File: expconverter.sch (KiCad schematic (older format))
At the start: 23 parts, among them IC2 LM324, IC4 LM324, P1 100k, P2 100k, P3 100k log, P7 200, P8 100k

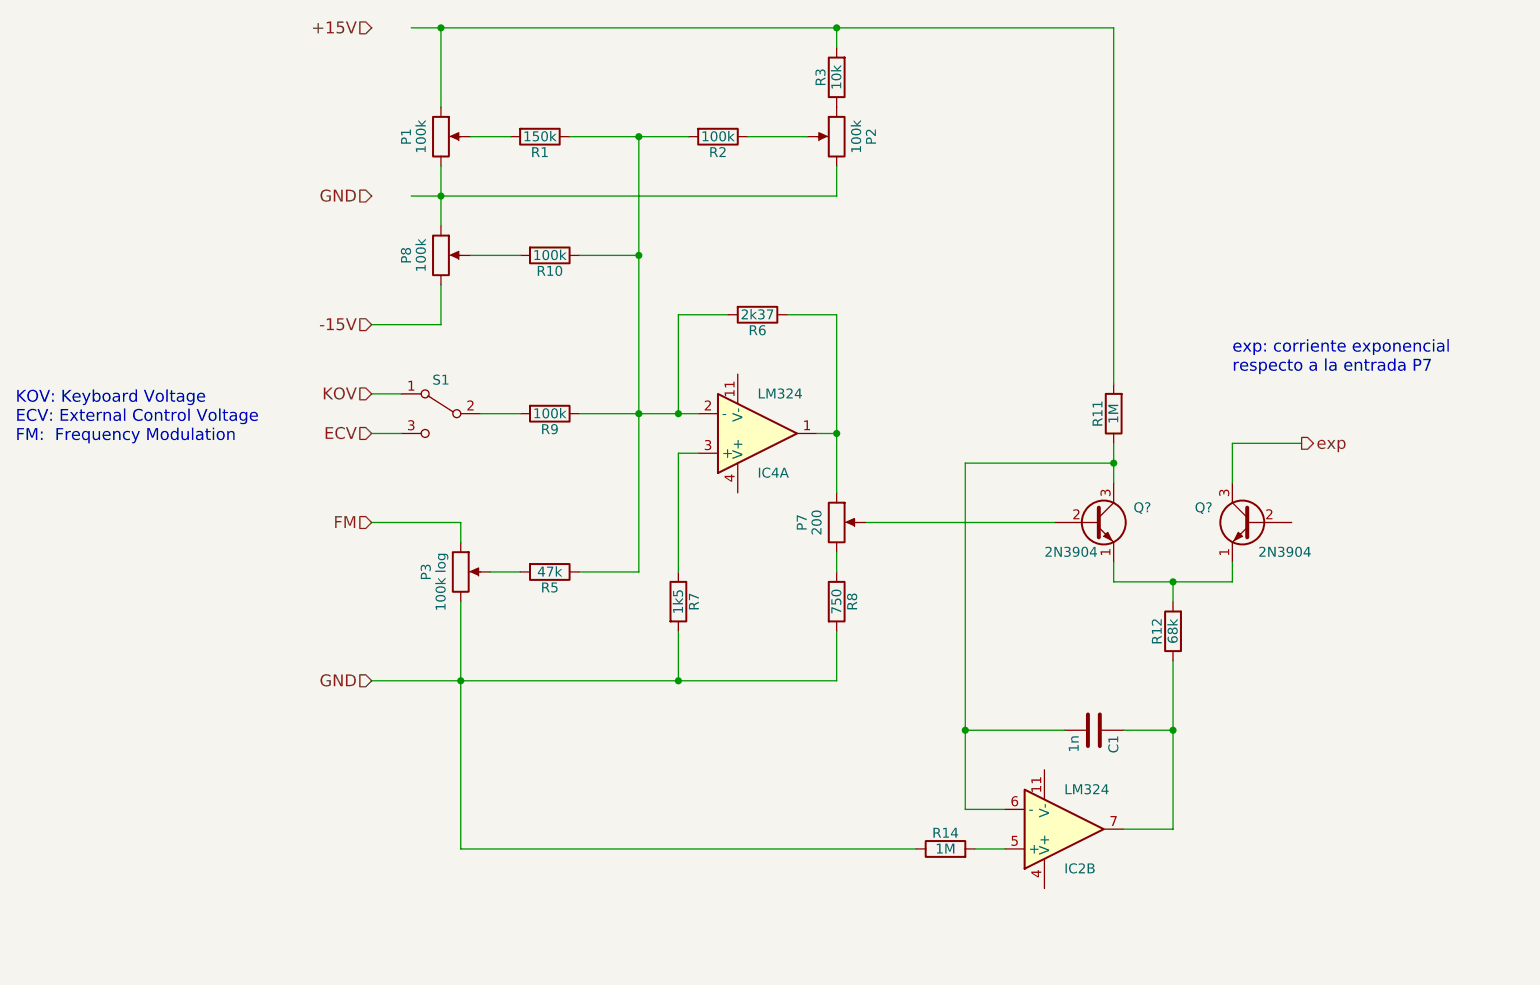
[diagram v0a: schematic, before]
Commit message: sawtooh 2 triangle
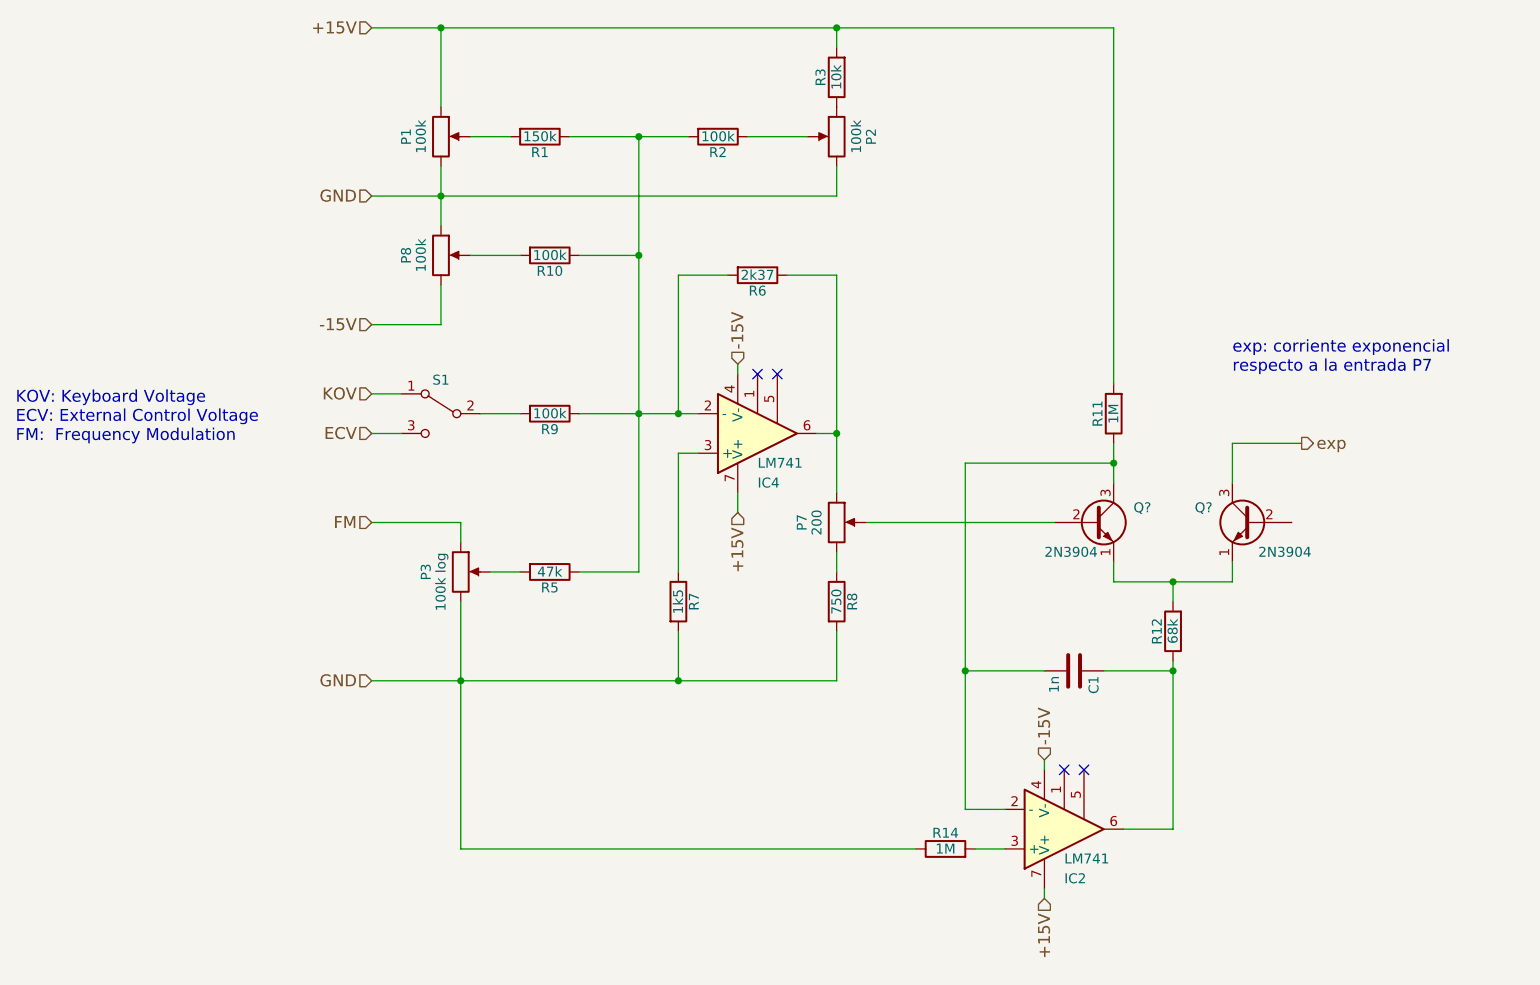
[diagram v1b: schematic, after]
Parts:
- removed IC2, IC4: LM324, symbol LM324
- added IC2, IC4: LM741, symbol LM741
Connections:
- wire segments 53 -> 57
- no-connect marks 0 -> 4
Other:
- moved on the sheet: C1, R6
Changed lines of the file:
@@
 $EndDescr
-$Comp
-L LM324 IC4
-U 1 1 59D555A7
-P 6800 3400
-F 0 "IC4" H 6800 3600 50  0000 L CNN
-F 1 "LM324" H 6800 3200 50  0000 L CNN
-F 2 "" H 6750 3500 50  0001 C CNN
-F 3 "" H 6850 3600 50  0001 C CNN
-	1    6800 3400
-	1    0    0    1
-$EndComp
 $Comp
 L R R6
 U 1 1 59D555CD
-P 6800 2800
-F 0 "R6" V 6880 2800 50  0000 C CNN
-F 1 "2k37" V 6800 2800 50  0000 C CNN
-F 2 "" V 6730 2800 50  0001 C CNN
-F 3 "" H 6800 2800 50  0001 C CNN
-	1    6800 2800
+P 6800 2600
+F 0 "R6" V 6880 2600 50  0000 C CNN
+F 1 "2k37" V 6800 2600 50  0000 C CNN
+F 2 "" V 6730 2600 50  0001 C CNN
+F 3 "" H 6800 2600 50  0001 C CNN
+	1    6800 2600
 	0    1    1    0
 $EndComp
@@
 	4850 3200 5000 3200
 Wire Wire Line
-	6650 2800 6400 2800
-Wire Wire Line
-	6400 2800 6400 3300
+	6650 2600 6400 2600
+Wire Wire Line
+	6400 2600 6400 3300
 Connection ~ 6400 3300
 Wire Wire Line
-	6950 2800 7200 2800
-Wire Wire Line
-	7200 2800 7200 3700
+	6950 2600 7200 2600
+Wire Wire Line
+	7200 2600 7200 3700
 Wire Wire Line
 	7200 3400 7100 3400
@@
 	5200 2050 5200 2350
 Wire Wire Line
-	5050 2200 7200 2200
+	4850 2200 7200 2200
 Connection ~ 5200 2200
 Wire Wire Line
@@
 	5200 1750 5200 1350
 Wire Wire Line
-	5050 1350 8600 1350
+	4850 1350 8600 1350
 Wire Wire Line
 	7200 1350 7200 1450
@@
 $EndComp
 $Comp
-L LM324 IC2
-U 2 1 59D5AC51
-P 8350 5400
-F 0 "IC2" H 8350 5600 50  0000 L CNN
-F 1 "LM324" H 8350 5200 50  0000 L CNN
-F 2 "" H 8300 5500 50  0001 C CNN
-F 3 "" H 8400 5600 50  0001 C CNN
-	2    8350 5400
-	1    0    0    1
-$EndComp
-$Comp
 L R R14
 U 1 1 59D5ACFD
@@
 L C C1
 U 1 1 59D5AF78
-P 8500 4900
-F 0 "C1" H 8525 5000 50  0000 L CNN
-F 1 "1n" H 8525 4800 50  0000 L CNN
-F 2 "" H 8538 4750 50  0001 C CNN
-F 3 "" H 8500 4900 50  0001 C CNN
-	1    8500 4900
+P 8400 4600
+F 0 "C1" H 8425 4700 50  0000 L CNN
+F 1 "1n" H 8425 4500 50  0000 L CNN
+F 2 "" H 8438 4450 50  0001 C CNN
+F 3 "" H 8400 4600 50  0001 C CNN
+	1    8400 4600
 	0    1    1    0
 $EndComp
@@
 Connection ~ 8900 4150
 Wire Wire Line
-	7850 4900 8350 4900
-Wire Wire Line
-	8650 4900 8900 4900
+	7850 4600 8250 4600
+Wire Wire Line
+	8550 4600 8900 4600
 Wire Wire Line
 	8900 4550 8900 5400
 Wire Wire Line
 	8900 5400 8650 5400
-Connection ~ 8900 4900
+Connection ~ 8900 4600
 Wire Wire Line
 	7350 3850 8300 3850
@@
 	5300 5500 7600 5500
 Wire Wire Line
-	8600 3650 8600 3450
+	8600 3450 8600 3650
 Wire Wire Line
 	7850 3550 8600 3550
 Connection ~ 8600 3550
-Connection ~ 7850 4900
+Connection ~ 7850 4600
 Wire Wire Line
 	8600 1350 8600 3150
@@
 Text Notes 9200 3100 0    60   ~ 0
 exp: corriente exponencial \nrespecto a la entrada P7
+$Comp
+L LM741 IC4
+U 1 1 59D5EB1B
+P 6800 3400
+F 0 "IC4" H 6800 3650 50  0000 L CNN
+F 1 "LM741" H 6800 3550 50  0000 L CNN
+F 2 "" H 6850 3450 50  0001 C CNN
+F 3 "" H 6950 3550 50  0001 C CNN
+	1    6800 3400
+	1    0    0    1
+$EndComp
+Text HLabel 6700 3800 3    60   Input ~ 0
++15V
+Wire Wire Line
+	6700 3700 6700 3800
+Text HLabel 6700 3050 1    60   Input ~ 0
+-15V
+Wire Wire Line
+	6700 3100 6700 3050
+NoConn ~ 6800 3100
+NoConn ~ 6900 3100
+$Comp
+L LM741 IC2
+U 1 1 59D5F4FC
+P 8350 5400
+F 0 "IC2" H 8350 5650 50  0000 L CNN
+F 1 "LM741" H 8350 5550 50  0000 L CNN
+F 2 "" H 8400 5450 50  0001 C CNN
+F 3 "" H 8500 5550 50  0001 C CNN
+	1    8350 5400
+	1    0    0    1
+$EndComp
+Text HLabel 8250 5750 3    60   Input ~ 0
++15V
+Text HLabel 8250 5050 1    60   Input ~ 0
+-15V
+Wire Wire Line
+	8250 5100 8250 5050
+Wire Wire Line
+	8250 5750 8250 5700
+NoConn ~ 8350 5100
+NoConn ~ 8450 5100
 $EndSCHEMATC
